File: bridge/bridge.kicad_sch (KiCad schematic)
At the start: 25 parts, among them Q1 STGP7NC60HD, Q2 STGP7NC60HD, Q3 STGP7NC60HD, Q4 STGP7NC60HD, T1 P0926NL, T2 P0926NL

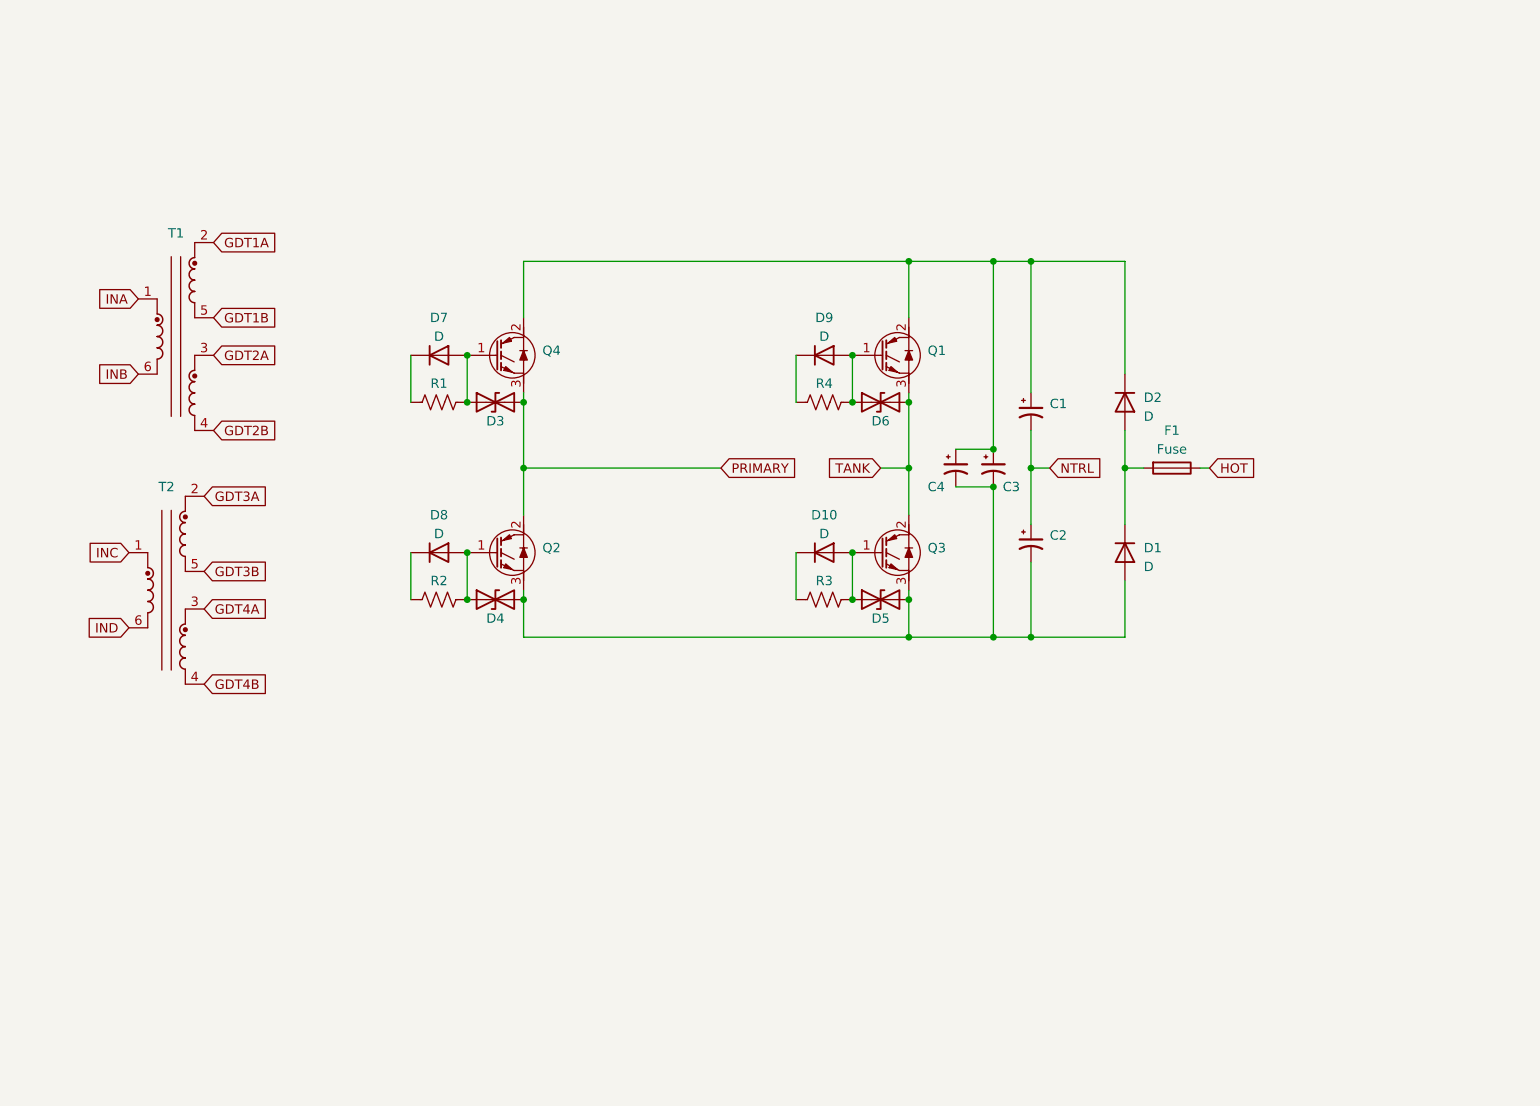
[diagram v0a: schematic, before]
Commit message: finish basic bridge, remove voltage doubler
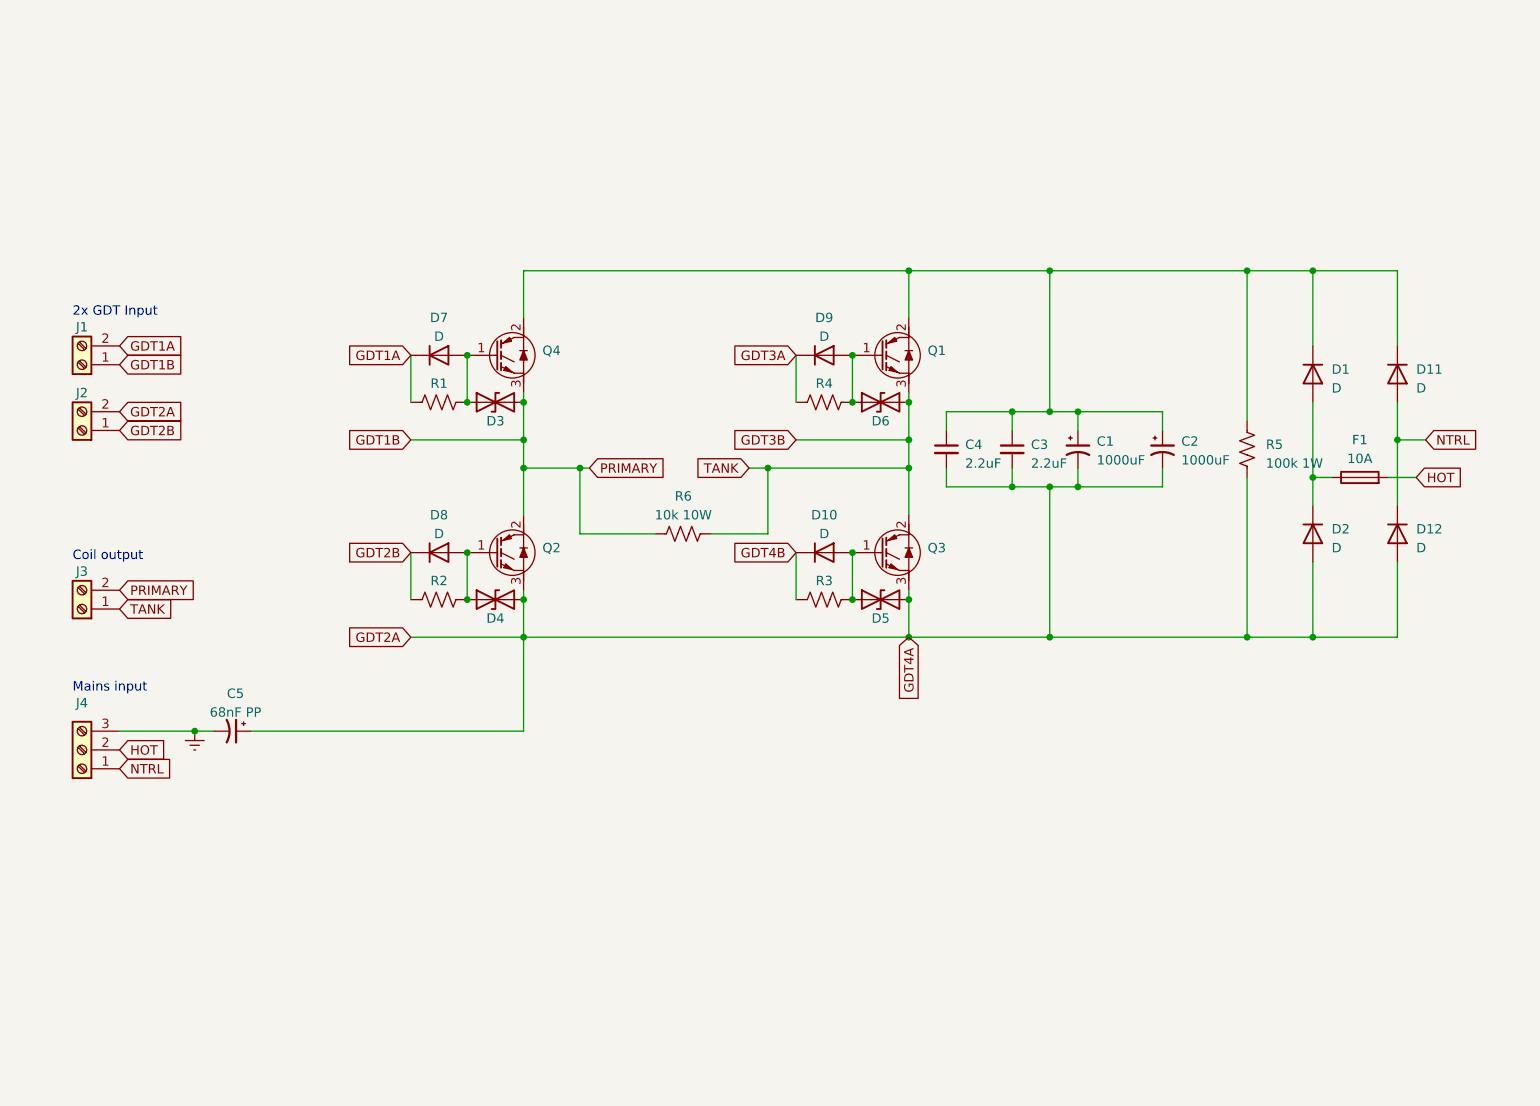
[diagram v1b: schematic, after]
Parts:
- removed C3, C4: C_Polarized_Small_US, symbol Device:C_Polarized_Small_US
- removed T1, T2: P0926NL, Transformer_SMD:Pulse_P0926NL, symbol Transformer:P0926NL
- added C3, C4: 2.2uF, symbol Device:C_Small
- added C5: 68nF PP, symbol Device:C_Polarized_Small_US
- added D11, D12: D, symbol Device:D
- added J1, J2, J3: Screw_Terminal_01x02, symbol Connector:Screw_Terminal_01x02
- added J4: Screw_Terminal_01x03, symbol Connector:Screw_Terminal_01x03
- added R5: 100k 1W, symbol Device:R_US
- added R6: 10k 10W, symbol Device:R_US
- C1, C2: value C_Polarized_Small_US -> 1000uF
- F1: value Fuse -> 10A
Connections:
- net PRIMARY is gone; now on net GDT1B: D3.2 (A2), Q2.2 (C), Q4.3 (E)
- net TANK is gone; now on net GDT3B: D6.2 (A2), Q1.3 (E), Q3.2 (C)
- net GDT1A: now also D7.1 (K), R1.2, J1.2 (Pin_2)
- net GDT1B: now also J1.1 (Pin_1), J3.2 (Pin_2), R6.2
- net GDT2A: now also C1.2, C2.2, D2.2 (A), D4.2 (A2), D5.2 (A2), Q2.3 (E), Q3.3 (E), C3.2, C4.2, C5.1, D12.2 (A), J2.2 (Pin_2), R5.2
- net GDT2B: now also D8.1 (K), R2.2, J2.1 (Pin_1)
- net GDT3A: now also D9.1 (K), R4.2
- net GDT3B: now also J3.1 (Pin_1), R6.1
- net GDT4B: now also D10.1 (K), R3.2
- net HOT: now also F1.2, J4.2 (Pin_2); no longer F1.1
- net NTRL: now also D11.2 (A), D12.1 (K), J4.1 (Pin_1); no longer C1.2, C2.1
- net at C1.1, Q1.2 (C), Q4.2 (C): now also C2.1, D1.1 (K), C3.1, C4.1, D11.1 (K), R5.1; no longer D2.1 (K)
- new net: D1.2 (A), D2.1 (K), F1.1
- new net Earth: C5.2, J4.3 (Pin_3)
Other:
- note added: "2x GDT Input"
- note added: "Coil output"
- note added: "Mains input"

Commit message: bridge footprints done
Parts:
- removed D1, D11, D12, D2: D, symbol Device:D
- added D9: GBPC3510W, conn:DIOB_GBPC3510W, symbol GBPC3510W:GBPC3510W
- C1: renamed from C5; footprint (none) -> Capacitor_THT:C_Rect_L18.0mm_W9.0mm_P15.00mm_FKS3_FKP3
- C2: renamed from C4; footprint (none) -> Capacitor_THT:C_Rect_L26.5mm_W11.5mm_P22.50mm_MKS4
- C3: footprint (none) -> Capacitor_THT:C_Rect_L26.5mm_W11.5mm_P22.50mm_MKS4
- C4: renamed from C1; footprint (none) -> Capacitor_THT:CP_Radial_D35.0mm_P10.00mm_SnapIn
- C5: renamed from C2; footprint (none) -> Capacitor_THT:CP_Radial_D35.0mm_P10.00mm_SnapIn
- D1: renamed from D7; footprint (none) -> Diode_SMD:D_SOD-123F
- D2: renamed from D8; footprint (none) -> Diode_SMD:D_SOD-123F
- D3, D4: footprint (none) -> Diode_SMD:D_SMA
- D5: renamed from D9; footprint (none) -> Diode_SMD:D_SOD-123F
- D6: renamed from D10; footprint (none) -> Diode_SMD:D_SOD-123F
- D7: renamed from D6; footprint (none) -> Diode_SMD:D_SMA
- D8: renamed from D5; footprint (none) -> Diode_SMD:D_SMA
- F1: footprint (none) -> conn:696108003002
- J1, J2, J3: footprint (none) -> conn:PHOENIX_1935161
- J4: footprint (none) -> conn:PHOENIX_1935174
- Q1: renamed from Q4; footprint Package_TO_SOT_THT:TO-220-3_Vertical -> Package_TO_SOT_THT:TO-3P-3_Horizontal_TabDown
- Q2: footprint Package_TO_SOT_THT:TO-220-3_Vertical -> Package_TO_SOT_THT:TO-3P-3_Horizontal_TabDown
- Q3: renamed from Q1; footprint Package_TO_SOT_THT:TO-220-3_Vertical -> Package_TO_SOT_THT:TO-3P-3_Horizontal_TabDown
- Q4: renamed from Q3; footprint Package_TO_SOT_THT:TO-220-3_Vertical -> Package_TO_SOT_THT:TO-3P-3_Horizontal_TabDown
- R1, R2, R4: footprint (none) -> Resistor_SMD:R_1206_3216Metric_Pad1.30x1.75mm_HandSolder
- R3: renamed from R6; footprint (none) -> Resistor_THT:R_Axial_Shunt_L22.2mm_W8.0mm_PS14.30mm_P25.40mm
- R5: renamed from R3; footprint (none) -> Resistor_SMD:R_1206_3216Metric_Pad1.30x1.75mm_HandSolder
- R6: renamed from R5; footprint (none) -> Resistor_THT:R_Axial_DIN0207_L6.3mm_D2.5mm_P7.62mm_Horizontal
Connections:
- net GDT2A: now also D9.-
- net NTRL: now also D9.AC1
- net at C2.1, C3.1, C4.1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: now also D9.+
- net at F1.1: now also D9.AC2
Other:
- moved on the sheet: F1

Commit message: fix bridge, still figuring out layout
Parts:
- removed J3: Screw_Terminal_01x02, conn:PHOENIX_1935161, symbol Connector:Screw_Terminal_01x02
- added H1, H2, H3, H4, H5, H6: MountingHole_Pad, MountingHole:MountingHole_3.2mm_M3_Pad_Via, symbol Mechanical:MountingHole_Pad
- added J3, J5: Conn_01x01_Pin, conn:TE_1217861-1, symbol Connector:Conn_01x01_Pin
- added T1, T2: P0584NL, footprints:P0584NL_PUL, symbol 2023-05-30_04-28-53:P0584NL
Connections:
- net Earth: now also H1.1, H2.1, H3.1, H4.1, H5.1, H6.1
- net GDT1A: now also T1.8; no longer J1.2 (Pin_2)
- net GDT1B: now also J5.1 (Pin_1), T1.7; no longer J1.1 (Pin_1)
- net GDT2A: now also D2.1 (K), R2.2, T1.3; no longer C1.1, C2.2, C3.2, C4.2, C5.2, D4.2 (A2), D8.2 (A2), D9.-, J2.2 (Pin_2), Q2.3 (E), Q4.3 (E), R6.2
- net GDT2B: now also C1.1, C2.2, C3.2, C4.2, C5.2, D4.2 (A2), D8.2 (A2), D9.-, Q2.3 (E), Q4.3 (E), R6.2, T1.4, T2.4; no longer D2.1 (K), J2.1 (Pin_1), R2.2
- net GDT3A: now also T2.8
- net GDT3B: now also J3.1 (Pin_1), T2.7
- net GDT4B renamed GDT4A
- net GDT4A: now also T2.3
- new net: J1.2 (Pin_2), T1.1
- new net: J1.1 (Pin_1), T1.10
- new net: J2.1 (Pin_1), T2.10
- new net: J2.2 (Pin_2), T2.1
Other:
- note removed: "2x GDT Input"
- moved on the sheet: J1, J2
